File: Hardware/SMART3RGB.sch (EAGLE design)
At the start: 14 parts, among them IC1 WS2811-SOP8, IC2 WS2811-SOP8, IC3 WS2811-SOP8, IC4 WS2811-SOP8, SW1 QG16F-RGB, SW2 QG16F-RGB, SW3 QG16F-RGB, SW4 QG16F-RGB

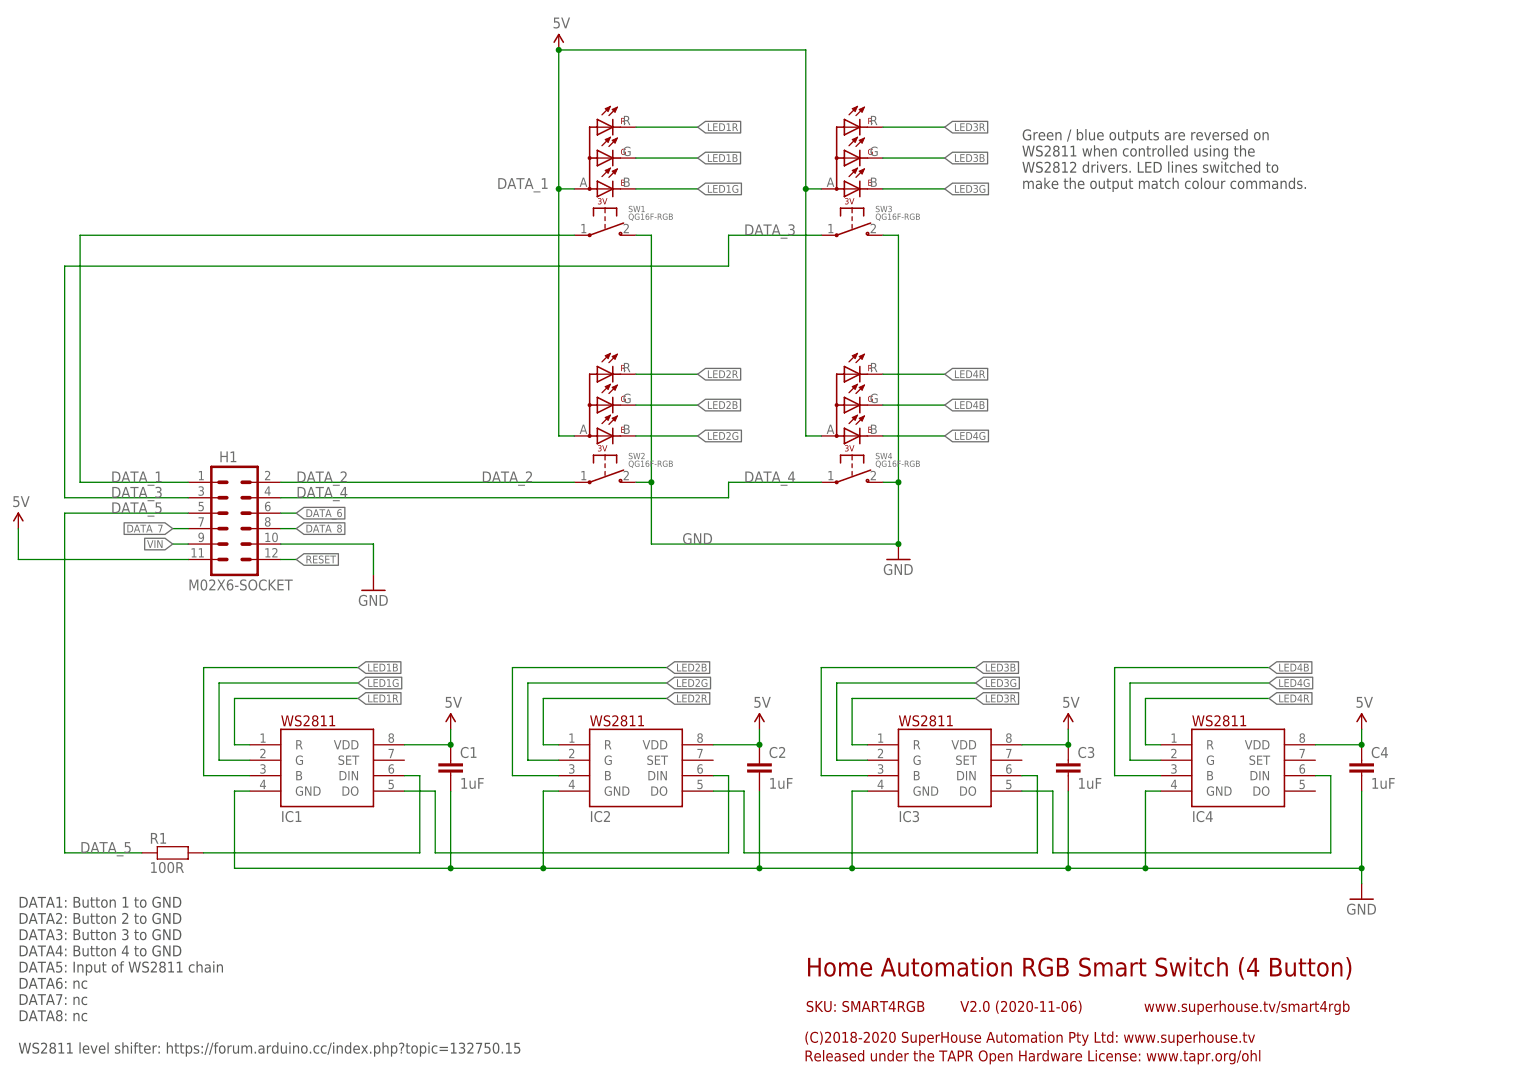
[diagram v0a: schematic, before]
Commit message: Routing, ERC, and DRC for v2.0 release.
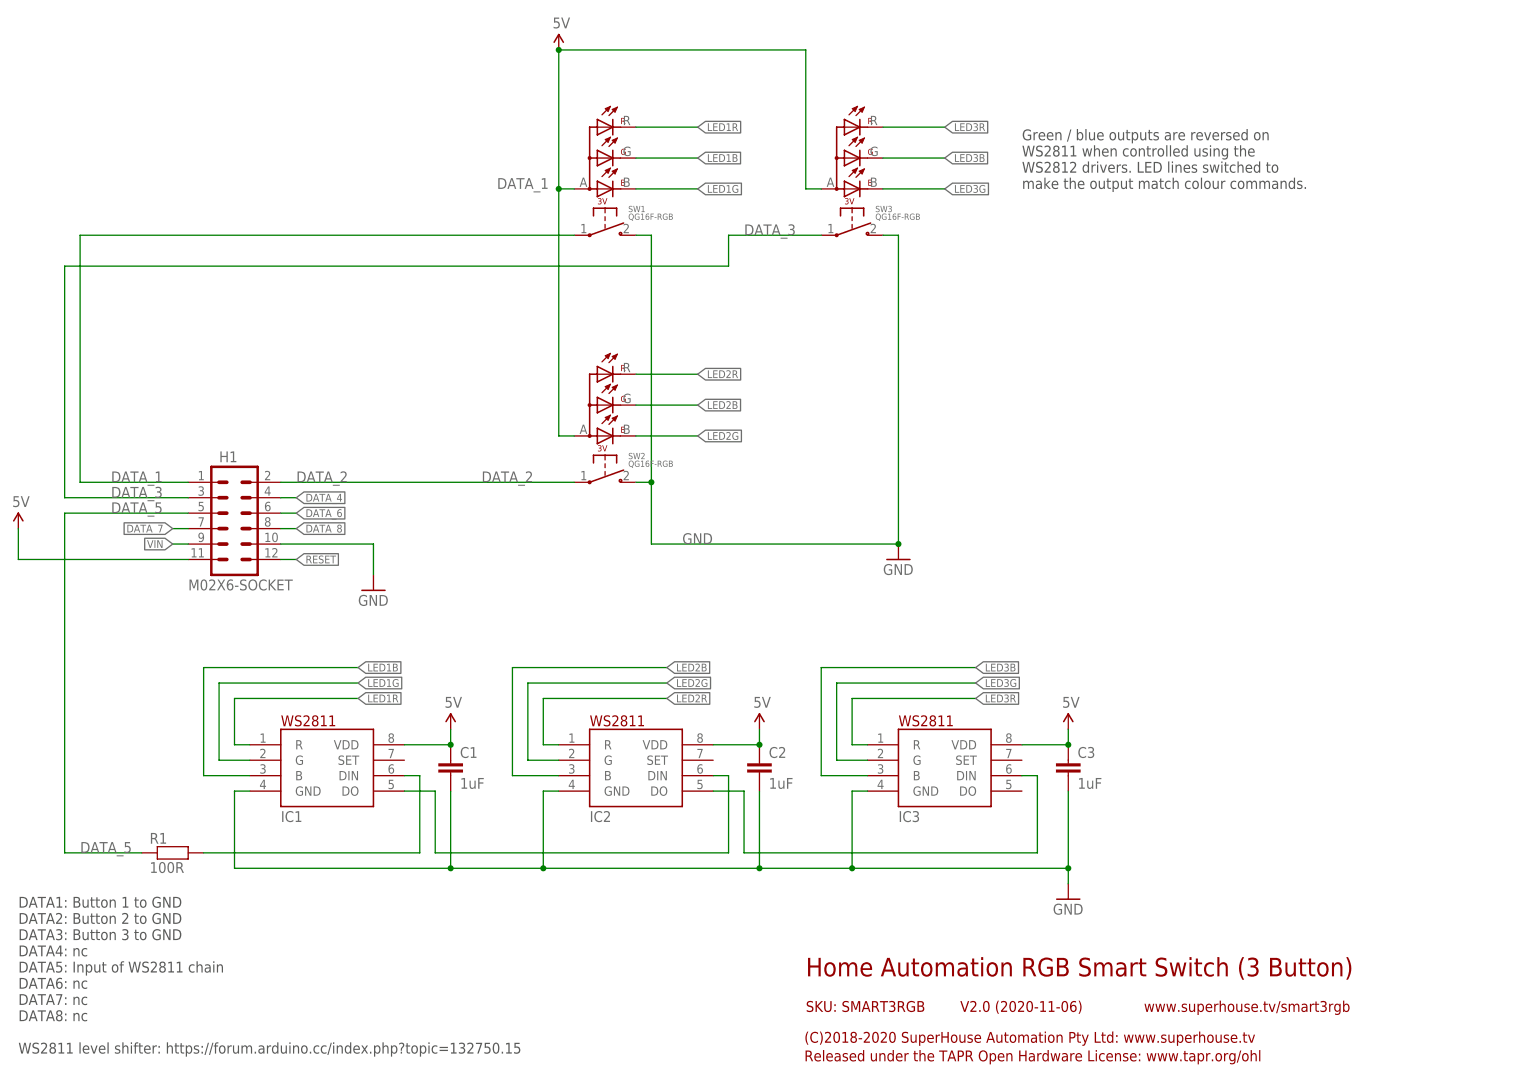
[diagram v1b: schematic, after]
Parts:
- removed C4: 1uF, SuperHouse-DiscreteSemi:CAP0603
- removed IC4: WS2811-SOP8, SuperHouse-ICs:WS2811-SOP8
- removed SW4: QG16F-RGB, SuperHouse-Switches:QG16F-RGB
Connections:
- removed net LED4B: IC4.B, SW4.G
- removed net LED4G: IC4.G, SW4.B
- removed net LED4R: IC4.R, SW4.R
- removed net N$13: IC3.DO, IC4.DIN
- net 5V: no longer C4.1, IC4.VDD, SW4.+
- net DATA_4: no longer SW4.1
- net GND: no longer C4.2, IC4.GND, SW4.2
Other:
- note added: "DATA1: Button 1 to GND DATA2: Button 2 to GND DATA3: Button 3 to GND DATA4: nc DATA5: Input of WS2811 chain DATA6: nc DATA7: nc DATA8: nc WS2811 level shifter: https://forum.arduino.cc/index.php?topic=132750.15"
- note added: "Home Automation RGB Smart Switch (3 Button)"
- note added: "SKU: SMART3RGB"
- note added: "www.superhouse.tv/smart3rgb"
- note removed: "DATA1: Button 1 to GND DATA2: Button 2 to GND DATA3: Button 3 to GND DATA4: Button 4 to GND DATA5: Input of WS2811 chain DATA6: nc DATA7: nc DATA8: nc WS2811 level shifter: https://forum.arduino.cc/index.php?topic=132750.15"
- note removed: "Home Automation RGB Smart Switch (4 Button)"
- note removed: "SKU: SMART4RGB"
- note removed: "www.superhouse.tv/smart4rgb"

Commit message: Converted switch isolation from FETs to diodes for v2.1 release.
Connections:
- net LED1B: now also SW1.B; no longer SW1.G
- net LED1G: now also IC1.R, SW1.G; no longer IC1.G, SW1.B
- net LED1R: now also IC1.G; no longer IC1.R
- net LED2B: now also SW2.B; no longer SW2.G
- net LED2G: now also IC2.R, SW2.G; no longer IC2.G, SW2.B
- net LED2R: now also IC2.G; no longer IC2.R
- net LED3B: now also SW3.B; no longer SW3.G
- net LED3G: now also IC3.R, SW3.G; no longer IC3.G, SW3.B
- net LED3R: now also IC3.G; no longer IC3.R
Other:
- note added: "Colours are mismatched on WS2811 when controlled using the WS2812 drivers. LED lines switched to make the output match colour commands."
- note added: "V2.1 (2020-12-23)"
- note removed: "Green / blue outputs are reversed on WS2811 when controlled using the WS2812 drivers. LED lines switched to make the output match colour commands."
- note removed: "V2.0 (2020-11-06)"
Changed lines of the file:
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@@
 <frame x1="0" y1="0" x2="248.92" y2="185.42" columns="8" rows="5" layer="94"/>
 <text x="139.7" y="20.32" size="3.048" layer="94">Home Automation RGB Smart Switch (3 Button)</text>
-<text x="165.1" y="14.478" size="1.778" layer="94">V2.0 (2020-11-06)</text>
+<text x="165.1" y="14.478" size="1.778" layer="94">V2.1 (2020-12-23)</text>
 <text x="139.7" y="14.478" size="1.778" layer="94">SKU: SMART3RGB</text>
 <text x="139.446" y="9.398" size="1.778" layer="94">(C)2018-2020 SuperHouse Automation Pty Ltd: www.superhouse.tv</text>
@@
 DATA8: nc
 WS2811 level shifter: https://forum.arduino.cc/index.php?topic=132750.15</text>
-<text x="175.26" y="149.86" size="1.778" layer="97">Green / blue outputs are reversed on
+<text x="175.26" y="149.86" size="1.778" layer="97">Colours are mismatched on
 WS2811 when controlled using the
 WS2812 drivers. LED lines switched to
@@
 </segment>
 <segment>
-<pinref part="SW1" gate="G$1" pin="G"/>
-<wire x1="111.76" y1="154.94" x2="121.92" y2="154.94" width="0.1524" layer="91"/>
-<label x="121.92" y="154.94" size="1.27" layer="95" xref="yes"/>
+<wire x1="111.76" y1="149.86" x2="121.92" y2="149.86" width="0.1524" layer="91"/>
+<pinref part="SW1" gate="G$1" pin="B"/>
+<label x="121.92" y="149.86" size="1.27" layer="95" xref="yes"/>
 </segment>
 </net>
@@
 </segment>
 <segment>
-<pinref part="SW2" gate="G$1" pin="G"/>
-<wire x1="111.76" y1="114.3" x2="121.92" y2="114.3" width="0.1524" layer="91"/>
-<label x="121.92" y="114.3" size="1.27" layer="95" xref="yes"/>
+<wire x1="111.76" y1="109.22" x2="121.92" y2="109.22" width="0.1524" layer="91"/>
+<pinref part="SW2" gate="G$1" pin="B"/>
+<label x="121.92" y="109.22" size="1.27" layer="95" xref="yes"/>
 </segment>
 </net>
@@
 </segment>
 <segment>
-<pinref part="SW3" gate="G$1" pin="G"/>
-<wire x1="152.4" y1="154.94" x2="162.56" y2="154.94" width="0.1524" layer="91"/>
-<label x="162.56" y="154.94" size="1.27" layer="95" xref="yes"/>
+<wire x1="152.4" y1="149.86" x2="162.56" y2="149.86" width="0.1524" layer="91"/>
+<pinref part="SW3" gate="G$1" pin="B"/>
+<label x="162.56" y="149.86" size="1.27" layer="95" xref="yes"/>
 </segment>
 </net>
@@
 </segment>
 <segment>
+<pinref part="IC1" gate="G$1" pin="G"/>
+<wire x1="48.26" y1="55.88" x2="43.18" y2="55.88" width="0.1524" layer="91"/>
+<wire x1="43.18" y1="55.88" x2="43.18" y2="68.58" width="0.1524" layer="91"/>
+<wire x1="43.18" y1="68.58" x2="66.04" y2="68.58" width="0.1524" layer="91"/>
+<label x="66.04" y="68.58" size="1.27" layer="95" xref="yes"/>
+</segment>
+</net>
+<net name="LED1G" class="0">
+<segment>
 <pinref part="IC1" gate="G$1" pin="R"/>
 <wire x1="48.26" y1="58.42" x2="45.72" y2="58.42" width="0.1524" layer="91"/>
@@
 <label x="66.04" y="66.04" size="1.27" layer="95" xref="yes"/>
 </segment>
-</net>
-<net name="LED1G" class="0">
-<segment>
-<pinref part="IC1" gate="G$1" pin="G"/>
-<wire x1="48.26" y1="55.88" x2="43.18" y2="55.88" width="0.1524" layer="91"/>
-<wire x1="43.18" y1="55.88" x2="43.18" y2="68.58" width="0.1524" layer="91"/>
-<wire x1="43.18" y1="68.58" x2="66.04" y2="68.58" width="0.1524" layer="91"/>
-<label x="66.04" y="68.58" size="1.27" layer="95" xref="yes"/>
-</segment>
-<segment>
-<wire x1="111.76" y1="149.86" x2="121.92" y2="149.86" width="0.1524" layer="91"/>
-<pinref part="SW1" gate="G$1" pin="B"/>
-<label x="121.92" y="149.86" size="1.27" layer="95" xref="yes"/>
+<segment>
+<pinref part="SW1" gate="G$1" pin="G"/>
+<wire x1="111.76" y1="154.94" x2="121.92" y2="154.94" width="0.1524" layer="91"/>
+<label x="121.92" y="154.94" size="1.27" layer="95" xref="yes"/>
 </segment>
 </net>
 <net name="LED3G" class="0">
+<segment>
+<pinref part="SW3" gate="G$1" pin="G"/>
+<wire x1="152.4" y1="154.94" x2="162.56" y2="154.94" width="0.1524" layer="91"/>
+<label x="162.56" y="154.94" size="1.27" layer="95" xref="yes"/>
+</segment>
+<segment>
+<pinref part="IC3" gate="G$1" pin="R"/>
+<wire x1="149.86" y1="58.42" x2="147.32" y2="58.42" width="0.1524" layer="91"/>
+<wire x1="147.32" y1="58.42" x2="147.32" y2="66.04" width="0.1524" layer="91"/>
+<wire x1="147.32" y1="66.04" x2="167.64" y2="66.04" width="0.1524" layer="91"/>
+<label x="167.64" y="66.04" size="1.27" layer="95" xref="yes"/>
+</segment>
+</net>
+<net name="LED3R" class="0">
+<segment>
+<pinref part="SW3" gate="G$1" pin="R"/>
+<wire x1="152.4" y1="160.02" x2="162.56" y2="160.02" width="0.1524" layer="91"/>
+<label x="162.56" y="160.02" size="1.27" layer="95" xref="yes"/>
+</segment>
 <segment>
 <pinref part="IC3" gate="G$1" pin="G"/>
@@
 <label x="167.64" y="68.58" size="1.27" layer="95" xref="yes"/>
 </segment>
-<segment>
-<wire x1="152.4" y1="149.86" x2="162.56" y2="149.86" width="0.1524" layer="91"/>
-<pinref part="SW3" gate="G$1" pin="B"/>
-<label x="162.56" y="149.86" size="1.27" layer="95" xref="yes"/>
-</segment>
-</net>
-<net name="LED3R" class="0">
-<segment>
-<pinref part="SW3" gate="G$1" pin="R"/>
-<wire x1="152.4" y1="160.02" x2="162.56" y2="160.02" width="0.1524" layer="91"/>
-<label x="162.56" y="160.02" size="1.27" layer="95" xref="yes"/>
-</segment>
-<segment>
-<pinref part="IC3" gate="G$1" pin="R"/>
-<wire x1="149.86" y1="58.42" x2="147.32" y2="58.42" width="0.1524" layer="91"/>
-<wire x1="147.32" y1="58.42" x2="147.32" y2="66.04" width="0.1524" layer="91"/>
-<wire x1="147.32" y1="66.04" x2="167.64" y2="66.04" width="0.1524" layer="91"/>
-<label x="167.64" y="66.04" size="1.27" layer="95" xref="yes"/>
-</segment>
 </net>
 <net name="LED2G" class="0">
+<segment>
+<pinref part="SW2" gate="G$1" pin="G"/>
+<wire x1="111.76" y1="114.3" x2="121.92" y2="114.3" width="0.1524" layer="91"/>
+<label x="121.92" y="114.3" size="1.27" layer="95" xref="yes"/>
+</segment>
+<segment>
+<pinref part="IC2" gate="G$1" pin="R"/>
+<wire x1="99.06" y1="58.42" x2="96.52" y2="58.42" width="0.1524" layer="91"/>
+<wire x1="96.52" y1="58.42" x2="96.52" y2="66.04" width="0.1524" layer="91"/>
+<wire x1="96.52" y1="66.04" x2="116.84" y2="66.04" width="0.1524" layer="91"/>
+<label x="116.84" y="66.04" size="1.27" layer="95" xref="yes"/>
+</segment>
+</net>
+<net name="LED2R" class="0">
+<segment>
+<pinref part="SW2" gate="G$1" pin="R"/>
+<wire x1="111.76" y1="119.38" x2="121.92" y2="119.38" width="0.1524" layer="91"/>
+<label x="121.92" y="119.38" size="1.27" layer="95" xref="yes"/>
+</segment>
 <segment>
 <pinref part="IC2" gate="G$1" pin="G"/>
@@
 <label x="116.84" y="68.58" size="1.27" layer="95" xref="yes"/>
 </segment>
-<segment>
-<wire x1="111.76" y1="109.22" x2="121.92" y2="109.22" width="0.1524" layer="91"/>
-<pinref part="SW2" gate="G$1" pin="B"/>
-<label x="121.92" y="109.22" size="1.27" layer="95" xref="yes"/>
-</segment>
-</net>
-<net name="LED2R" class="0">
-<segment>
-<pinref part="SW2" gate="G$1" pin="R"/>
-<wire x1="111.76" y1="119.38" x2="121.92" y2="119.38" width="0.1524" layer="91"/>
-<label x="121.92" y="119.38" size="1.27" layer="95" xref="yes"/>
-</segment>
-<segment>
-<pinref part="IC2" gate="G$1" pin="R"/>
-<wire x1="99.06" y1="58.42" x2="96.52" y2="58.42" width="0.1524" layer="91"/>
-<wire x1="96.52" y1="58.42" x2="96.52" y2="66.04" width="0.1524" layer="91"/>
-<wire x1="96.52" y1="66.04" x2="116.84" y2="66.04" width="0.1524" layer="91"/>
-<label x="116.84" y="66.04" size="1.27" layer="95" xref="yes"/>
-</segment>
-</net>
+</net>
